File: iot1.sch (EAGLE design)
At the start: 32 parts, among them IC1 MEGA8-P, IC2 7805T, J1 DCJ0202, U2 HTU21D, X1 22-23-2041, X2 A1944-50

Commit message: adc
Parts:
- added C14, C15: (no value), rcl:C-EUC0603
- added IC3: LTC2486C, linear-technology:LTC2486C
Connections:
- removed net N$29: IC1.PC4(ADC4/SDA)
- new net N$71: IC3.CH3
- new net N$74: IC3.CH2
- new net N$75: IC3.CH1
- new net N$76: IC3.CH0
- new net N$77: IC3.COM
- net 5V: now also C14.1, C15.1, IC3.VCC, IC3.VREF+
- net GND: now also C14.2, C15.2, IC3.!CS, IC3.EXP, IC3.GND, IC3.VREF-
- net N$31: now also IC3.SDO; no longer IC1.PC5(ADC5/SCL)
- net SCL: now also IC1.PC5(ADC5/SCL), IC3.FO, IC3.SCK
- net SDA: now also IC1.PC4(ADC4/SDA), IC3.SDI
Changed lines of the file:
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@@
 <part name="S1" library="switch-omron" library_urn="urn:adsk.eagle:library:377" deviceset="10-XX" device="" package3d_urn="urn:adsk.eagle:package:27496/1"/>
 <part name="C13" library="rcl" library_urn="urn:adsk.eagle:library:334" deviceset="C-EU" device="050-025X075" package3d_urn="urn:adsk.eagle:package:23637/1" value="0.1u"/>
+<part name="IC3" library="linear-technology" library_urn="urn:adsk.eagle:library:261" deviceset="LTC2486" device="" package3d_urn="urn:adsk.eagle:package:16069/1" technology="C"/>
+<part name="C14" library="rcl" library_urn="urn:adsk.eagle:library:334" deviceset="C-EU" device="C0603" package3d_urn="urn:adsk.eagle:package:23616/2"/>
+<part name="C15" library="rcl" library_urn="urn:adsk.eagle:library:334" deviceset="C-EU" device="C0603" package3d_urn="urn:adsk.eagle:package:23616/2"/>
 </parts>
 <sheets>
@@
 </segment>
 </net>
-<net name="N$29" class="0">
+<net name="SDA" class="0">
 <segment>
 <pinref part="IC1" gate="G$1" pin="PC4(ADC4/SDA)"/>
 <wire x1="162.56" y1="154.94" x2="187.96" y2="154.94" width="0.1524" layer="91"/>
-</segment>
-</net>
-<net name="N$31" class="0">
+<label x="190.5" y="154.94" size="1.778" layer="95"/>
+</segment>
+</net>
+<net name="SCL" class="0">
 <segment>
 <pinref part="IC1" gate="G$1" pin="PC5(ADC5/SCL)"/>
 <wire x1="162.56" y1="152.4" x2="187.96" y2="152.4" width="0.1524" layer="91"/>
+<label x="190.5" y="152.4" size="1.778" layer="95"/>
 </segment>
 </net>
@@
 <attribute name="NAME" x="69.723" y="135.1026" size="1.778" layer="95"/>
 <attribute name="VALUE" x="69.723" y="130.0226" size="1.778" layer="96"/>
+</instance>
+<instance part="IC3" gate="G$1" x="81.28" y="76.2" smashed="yes">
+<attribute name="NAME" x="73.66" y="92.71" size="1.778" layer="95"/>
+<attribute name="VALUE" x="73.66" y="58.42" size="1.778" layer="96"/>
+</instance>
+<instance part="C14" gate="G$1" x="33.02" y="76.2" smashed="yes" rot="R270">
+<attribute name="NAME" x="33.401" y="74.676" size="1.778" layer="95" rot="R270"/>
+<attribute name="VALUE" x="28.321" y="74.676" size="1.778" layer="96" rot="R270"/>
+</instance>
+<instance part="C15" gate="G$1" x="33.02" y="88.9" smashed="yes" rot="R270">
+<attribute name="NAME" x="33.401" y="87.376" size="1.778" layer="95" rot="R270"/>
+<attribute name="VALUE" x="28.321" y="87.376" size="1.778" layer="96" rot="R270"/>
 </instance>
 </instances>
@@
 <junction x="25.4" y="137.16"/>
 </segment>
+<segment>
+<pinref part="C15" gate="G$1" pin="2"/>
+<wire x1="27.94" y1="88.9" x2="22.86" y2="88.9" width="0.1524" layer="91"/>
+<pinref part="C14" gate="G$1" pin="2"/>
+<wire x1="22.86" y1="88.9" x2="22.86" y2="76.2" width="0.1524" layer="91"/>
+<wire x1="22.86" y1="76.2" x2="27.94" y2="76.2" width="0.1524" layer="91"/>
+<label x="20.32" y="71.12" size="1.778" layer="95"/>
+</segment>
+<segment>
+<pinref part="IC3" gate="G$1" pin="GND"/>
+<wire x1="71.12" y1="63.5" x2="58.42" y2="63.5" width="0.1524" layer="91"/>
+<label x="50.8" y="63.5" size="1.778" layer="95"/>
+</segment>
+<segment>
+<pinref part="IC3" gate="G$1" pin="!CS"/>
+<wire x1="71.12" y1="68.58" x2="58.42" y2="68.58" width="0.1524" layer="91"/>
+<label x="50.8" y="68.58" size="1.778" layer="95"/>
+</segment>
+<segment>
+<pinref part="IC3" gate="G$1" pin="VREF-"/>
+<wire x1="93.98" y1="83.82" x2="109.22" y2="83.82" width="0.1524" layer="91"/>
+<label x="111.76" y="83.82" size="1.778" layer="95"/>
+</segment>
+<segment>
+<pinref part="IC3" gate="G$1" pin="EXP"/>
+<wire x1="93.98" y1="63.5" x2="109.22" y2="63.5" width="0.1524" layer="91"/>
+<label x="111.76" y="63.5" size="1.778" layer="95"/>
+</segment>
 </net>
 <net name="SOIL_MOISTURE_1" class="0">
@@
 <wire x1="68.58" y1="142.24" x2="68.58" y2="137.16" width="0.1524" layer="91"/>
 </segment>
-</net>
+<segment>
+<pinref part="C14" gate="G$1" pin="1"/>
+<wire x1="35.56" y1="76.2" x2="40.64" y2="76.2" width="0.1524" layer="91"/>
+<pinref part="C15" gate="G$1" pin="1"/>
+<wire x1="35.56" y1="88.9" x2="40.64" y2="88.9" width="0.1524" layer="91"/>
+<wire x1="40.64" y1="88.9" x2="40.64" y2="76.2" width="0.1524" layer="91"/>
+<label x="40.64" y="91.44" size="1.778" layer="95"/>
+<pinref part="IC3" gate="G$1" pin="VCC"/>
+<wire x1="71.12" y1="88.9" x2="40.64" y2="88.9" width="0.1524" layer="91"/>
+<junction x="40.64" y="88.9"/>
+</segment>
+<segment>
+<pinref part="IC3" gate="G$1" pin="VREF+"/>
+<wire x1="93.98" y1="88.9" x2="109.22" y2="88.9" width="0.1524" layer="91"/>
+<label x="111.76" y="88.9" size="1.778" layer="95"/>
+</segment>
+</net>
+<net name="SDA" class="0">
+<segment>
+<pinref part="IC3" gate="G$1" pin="SDI"/>
+<wire x1="71.12" y1="78.74" x2="58.42" y2="78.74" width="0.1524" layer="91"/>
+<label x="50.8" y="78.74" size="1.778" layer="95"/>
+</segment>
+</net>
+<net name="N$31" class="0">
+<segment>
+<pinref part="IC3" gate="G$1" pin="SDO"/>
+<wire x1="71.12" y1="73.66" x2="58.42" y2="73.66" width="0.1524" layer="91"/>
+</segment>
+</net>
+<net name="N$71" class="0">
+<segment>
+<pinref part="IC3" gate="G$1" pin="CH3"/>
+<wire x1="93.98" y1="78.74" x2="109.22" y2="78.74" width="0.1524" layer="91"/>
+</segment>
+</net>
+<net name="N$74" class="0">
+<segment>
+<pinref part="IC3" gate="G$1" pin="CH2"/>
+<wire x1="93.98" y1="76.2" x2="109.22" y2="76.2" width="0.1524" layer="91"/>
+</segment>
+</net>
+<net name="N$75" class="0">
+<segment>
+<pinref part="IC3" gate="G$1" pin="CH1"/>
+<wire x1="93.98" y1="73.66" x2="109.22" y2="73.66" width="0.1524" layer="91"/>
+</segment>
+</net>
+<net name="N$76" class="0">
+<segment>
+<pinref part="IC3" gate="G$1" pin="CH0"/>
+<wire x1="93.98" y1="71.12" x2="109.22" y2="71.12" width="0.1524" layer="91"/>
+</segment>
+</net>
+<net name="N$77" class="0">
+<segment>
+<pinref part="IC3" gate="G$1" pin="COM"/>
+<wire x1="93.98" y1="66.04" x2="109.22" y2="66.04" width="0.1524" layer="91"/>
+</segment>
+</net>
+<net name="SCL" class="0">
+<segment>
+<pinref part="IC3" gate="G$1" pin="FO"/>
+<wire x1="71.12" y1="83.82" x2="58.42" y2="83.82" width="0.1524" layer="91"/>
+</segment>
+<segment>
+<pinref part="IC3" gate="G$1" pin="SCK"/>
+<wire x1="71.12" y1="76.2" x2="58.42" y2="76.2" width="0.1524" layer="91"/>
+<label x="50.8" y="76.2" size="1.778" layer="95"/>
+</segment>
+</net>

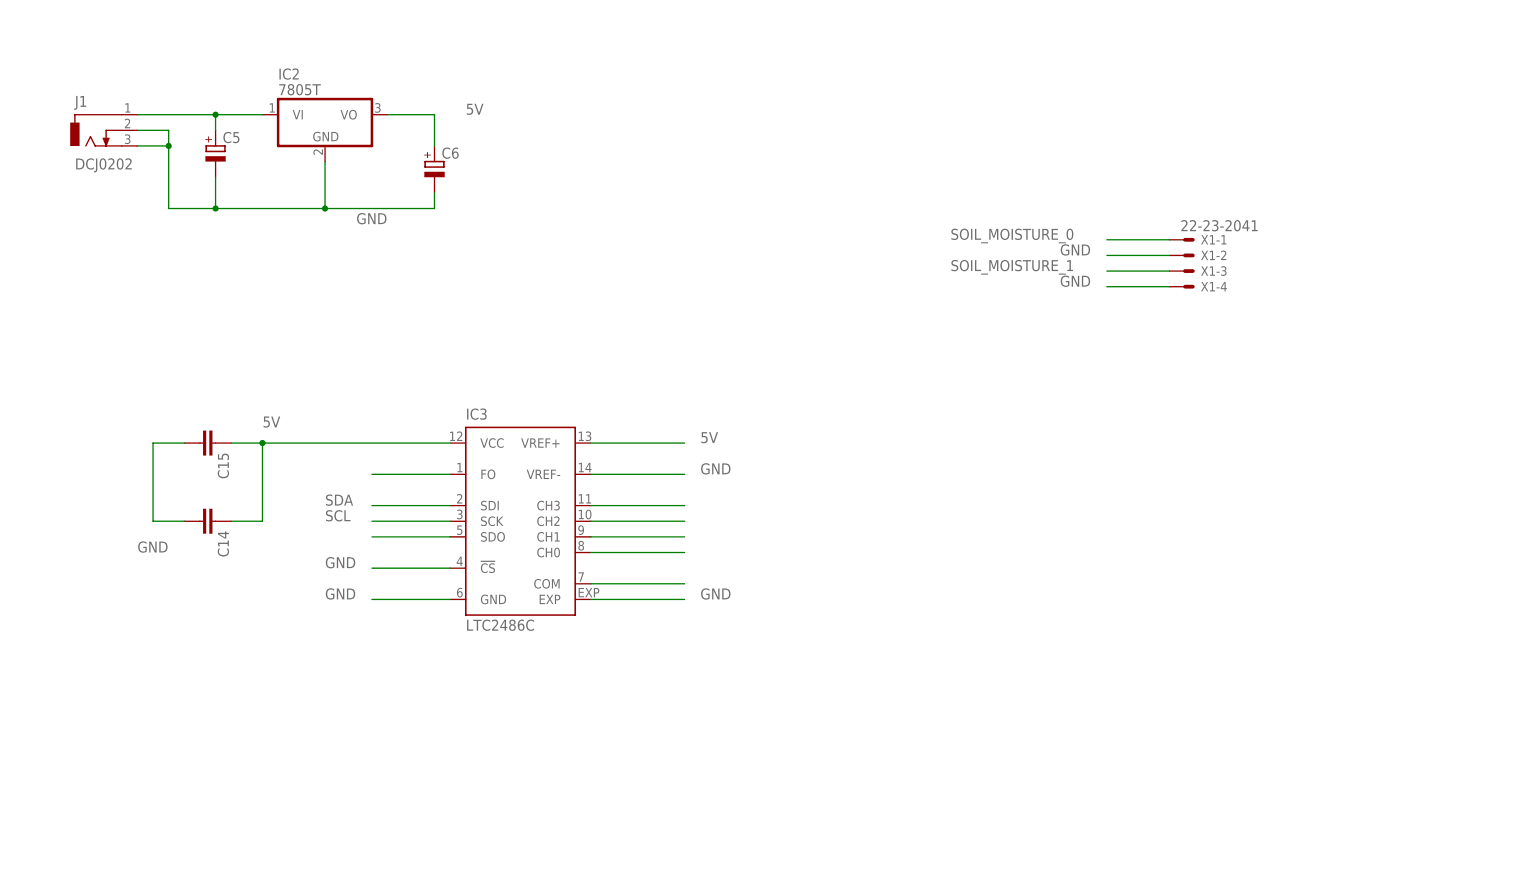
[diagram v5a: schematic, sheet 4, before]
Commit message: 3.3V regulator, multiplexer
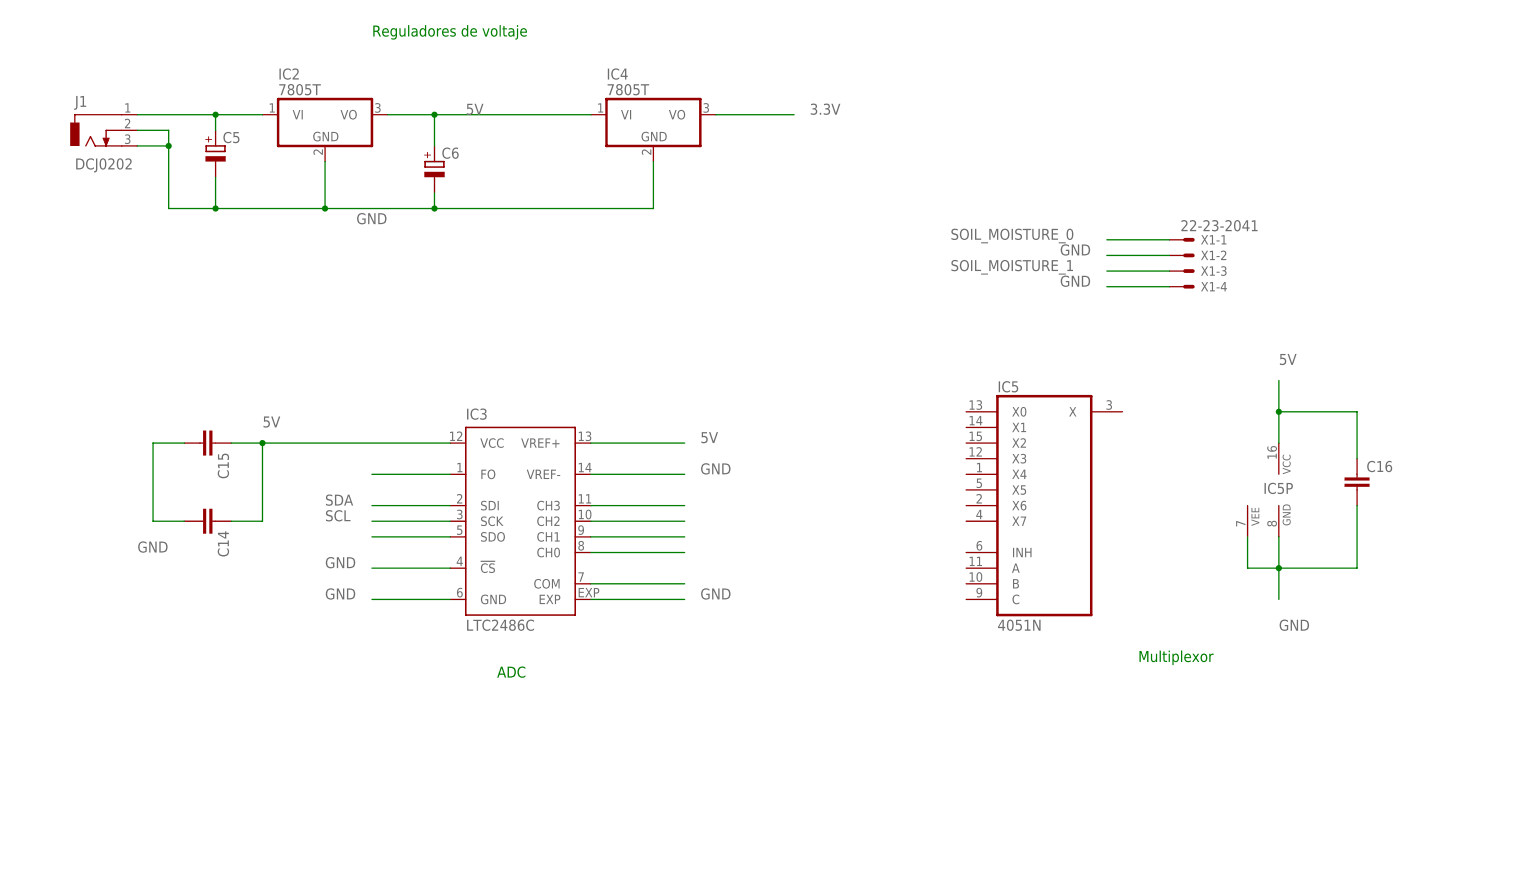
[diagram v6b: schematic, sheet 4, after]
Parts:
- added C16: (no value), rcl:C-EUC0603
- added IC4: 7805T, linear:7805T
- added IC5: 4051N, 40xx:4051N
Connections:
- net 3.3V: now also IC4.VO
- net 5V: now also C16.1, IC4.VI, IC5P.VCC
- net GND: now also C16.2, IC4.GND, IC5P.GND, IC5P.VEE
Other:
- note added: "ADC"
- note added: "Multiplexor"
- note added: "Reguladores de voltaje"
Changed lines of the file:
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@@
 <part name="C14" library="rcl" library_urn="urn:adsk.eagle:library:334" deviceset="C-EU" device="C0603" package3d_urn="urn:adsk.eagle:package:23616/2"/>
 <part name="C15" library="rcl" library_urn="urn:adsk.eagle:library:334" deviceset="C-EU" device="C0603" package3d_urn="urn:adsk.eagle:package:23616/2"/>
+<part name="IC4" library="linear" library_urn="urn:adsk.eagle:library:262" deviceset="78*" device="T" package3d_urn="urn:adsk.eagle:package:16414/1" technology="05"/>
+<part name="IC5" library="40xx" library_urn="urn:adsk.eagle:library:80" deviceset="4051" device="N" package3d_urn="urn:adsk.eagle:package:922/2"/>
+<part name="C16" library="rcl" library_urn="urn:adsk.eagle:library:334" deviceset="C-EU" device="C0603" package3d_urn="urn:adsk.eagle:package:23616/2"/>
 </parts>
 <sheets>
@@
 <sheet>
 <plain>
+<text x="182.88" y="53.34" size="1.778" layer="91">Multiplexor</text>
+<text x="78.74" y="50.8" size="1.778" layer="91">ADC</text>
+<text x="58.42" y="154.94" size="1.778" layer="91">Reguladores de voltaje</text>
 </plain>
 <instances>
@@
 <attribute name="NAME" x="33.401" y="87.376" size="1.778" layer="95" rot="R270"/>
 <attribute name="VALUE" x="28.321" y="87.376" size="1.778" layer="96" rot="R270"/>
+</instance>
+<instance part="IC4" gate="A1" x="104.14" y="142.24" smashed="yes">
+<attribute name="NAME" x="96.52" y="147.955" size="1.778" layer="95"/>
+<attribute name="VALUE" x="96.52" y="145.415" size="1.778" layer="96"/>
+</instance>
+<instance part="IC5" gate="A" x="167.64" y="78.74" smashed="yes">
+<attribute name="NAME" x="160.02" y="97.155" size="1.778" layer="95"/>
+<attribute name="VALUE" x="160.02" y="58.42" size="1.778" layer="96"/>
+</instance>
+<instance part="IC5" gate="P" x="205.74" y="81.28" smashed="yes">
+<attribute name="NAME" x="203.2" y="80.645" size="1.778" layer="95"/>
+</instance>
+<instance part="C16" gate="G$1" x="218.44" y="83.82" smashed="yes">
+<attribute name="NAME" x="219.964" y="84.201" size="1.778" layer="95"/>
+<attribute name="VALUE" x="219.964" y="79.121" size="1.778" layer="96"/>
 </instance>
 </instances>
@@
 <wire x1="25.4" y1="137.16" x2="25.4" y2="127" width="0.1524" layer="91"/>
 <junction x="25.4" y="137.16"/>
+<wire x1="68.58" y1="127" x2="104.14" y2="127" width="0.1524" layer="91"/>
+<junction x="68.58" y="127"/>
+<pinref part="IC4" gate="A1" pin="GND"/>
+<wire x1="104.14" y1="127" x2="104.14" y2="134.62" width="0.1524" layer="91"/>
 </segment>
 <segment>
@@
 <wire x1="93.98" y1="63.5" x2="109.22" y2="63.5" width="0.1524" layer="91"/>
 <label x="111.76" y="63.5" size="1.778" layer="95"/>
+</segment>
+<segment>
+<pinref part="C16" gate="G$1" pin="2"/>
+<wire x1="218.44" y1="78.74" x2="218.44" y2="68.58" width="0.1524" layer="91"/>
+<pinref part="IC5" gate="P" pin="GND"/>
+<wire x1="218.44" y1="68.58" x2="205.74" y2="68.58" width="0.1524" layer="91"/>
+<wire x1="205.74" y1="68.58" x2="205.74" y2="73.66" width="0.1524" layer="91"/>
+<pinref part="IC5" gate="P" pin="VEE"/>
+<wire x1="205.74" y1="68.58" x2="200.66" y2="68.58" width="0.1524" layer="91"/>
+<wire x1="200.66" y1="68.58" x2="200.66" y2="73.66" width="0.1524" layer="91"/>
+<junction x="205.74" y="68.58"/>
+<wire x1="205.74" y1="68.58" x2="205.74" y2="63.5" width="0.1524" layer="91"/>
+<label x="205.74" y="58.42" size="1.778" layer="95"/>
 </segment>
 </net>
@@
 <wire x1="60.96" y1="142.24" x2="68.58" y2="142.24" width="0.1524" layer="91"/>
 <wire x1="68.58" y1="142.24" x2="68.58" y2="137.16" width="0.1524" layer="91"/>
+<pinref part="IC4" gate="A1" pin="VI"/>
+<wire x1="68.58" y1="142.24" x2="93.98" y2="142.24" width="0.1524" layer="91"/>
+<junction x="68.58" y="142.24"/>
 </segment>
 <segment>
@@
 <label x="111.76" y="88.9" size="1.778" layer="95"/>
 </segment>
+<segment>
+<pinref part="IC5" gate="P" pin="VCC"/>
+<wire x1="205.74" y1="88.9" x2="205.74" y2="93.98" width="0.1524" layer="91"/>
+<pinref part="C16" gate="G$1" pin="1"/>
+<wire x1="205.74" y1="93.98" x2="218.44" y2="93.98" width="0.1524" layer="91"/>
+<wire x1="218.44" y1="93.98" x2="218.44" y2="86.36" width="0.1524" layer="91"/>
+<wire x1="205.74" y1="93.98" x2="205.74" y2="99.06" width="0.1524" layer="91"/>
+<junction x="205.74" y="93.98"/>
+<label x="205.74" y="101.6" size="1.778" layer="95"/>
+</segment>
 </net>
 <net name="SDA" class="0">
@@
 </segment>
 </net>
+<net name="3.3V" class="0">
+<segment>
+<pinref part="IC4" gate="A1" pin="VO"/>
+<wire x1="114.3" y1="142.24" x2="127" y2="142.24" width="0.1524" layer="91"/>
+<label x="129.54" y="142.24" size="1.778" layer="95"/>
+</segment>
+</net>

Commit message: 1Hz filter
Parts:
- added C17: (no value), rcl:C-EUC0603
- added D1, D2: 1N4004, diode:1N4004
- added R6: (no value), rcl:R-EU_0207/10
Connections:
- removed net N$76: IC3.CH0
- new net MUX_0: IC5A.A
- new net MUX_1: IC5A.B
- new net MUX_2: IC5A.C
- new net N$29: IC5A.X3
- new net N$36: IC5A.X4
- new net N$50: IC5A.X5
- new net N$65: IC5A.X6
- new net N$66: IC5A.X7
- new net N$9: IC5A.X2
- new net S: D1.A, D2.C, IC5A.X, R6.1
- new net SENSORS: C17.1, IC3.CH0, R6.2
- net 5V: now also D1.C
- net GND: now also C17.2, D2.A, IC5A.INH
- net SOIL_MOISTURE_0: now also IC5A.X0
- net SOIL_MOISTURE_1: now also IC5A.X1

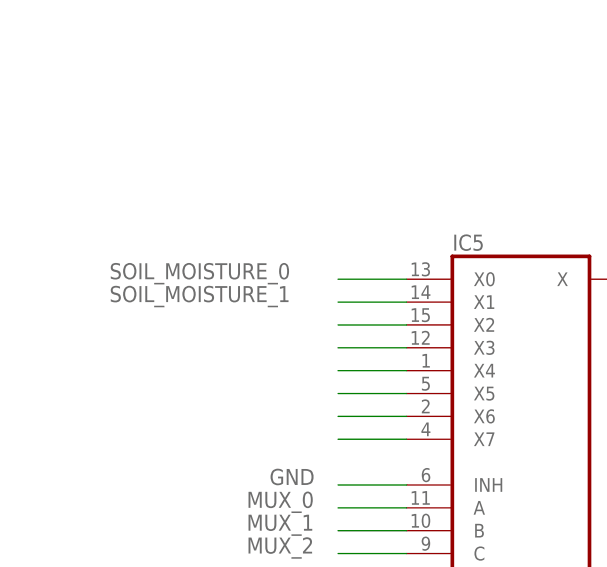
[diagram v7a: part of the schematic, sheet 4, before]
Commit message: 4-20ma amplification for soil moisture sensors
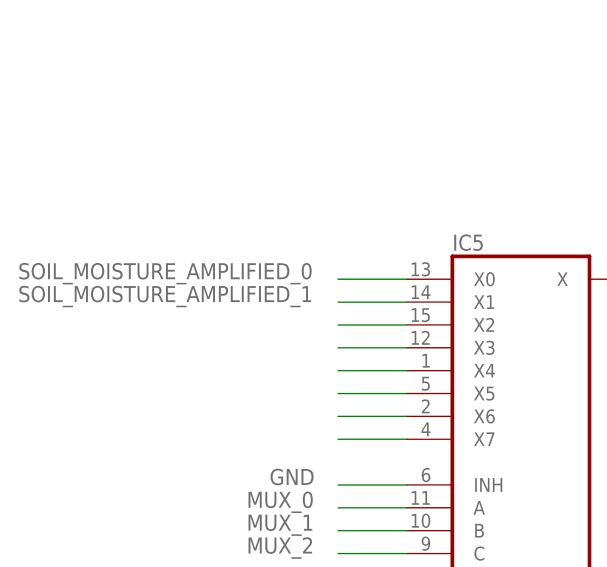
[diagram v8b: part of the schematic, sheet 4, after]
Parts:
- added IC6: OPA2134PA, linear:OPA2134PA
- added R12, R13, R14, R15, R16, R17, R18, R19, R20, R21: (no value), rcl:R-EU_0207/10
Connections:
- new net N$78: IC6A.+IN, R12.1, R16.2
- new net N$81: IC6A.-IN, R14.2
- new net N$82: IC6B.+IN, R20.1, R21.2
- new net N$83: IC6B.-IN, R18.2
- new net SOIL_MOISTURE_AMPLIFIED_0: IC5A.X0, IC6A.OUT, R12.2, R13.2
- new net SOIL_MOISTURE_AMPLIFIED_1: IC5A.X1, IC6B.OUT, R19.2, R20.2
- net 5V: now also IC6A.V+, R15.1, R17.1
- net GND: now also IC6A.V-, R16.1, R21.1
- net SOIL_MOISTURE_0: now also R13.1, R14.1, R15.2; no longer IC5A.X0
- net SOIL_MOISTURE_1: now also R17.2, R18.1, R19.1; no longer IC5A.X1
